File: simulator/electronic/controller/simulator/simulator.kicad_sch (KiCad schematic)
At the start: 9 parts, among them J1 Mover1, J2 Conn_01x06_Pin, J3 Conn_01x06_Pin, J4 Mover2, J5 Conn_01x06_Pin, J6 Rotator, J7 Conn_01x06_Pin, J8 Mover3, U1 ESP32 D1 Mini

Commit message: design schematics
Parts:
- removed J1: Mover1, Connector_JST:JST_XH_B6B-XH-A_1x06_P2.50mm_Vertical, symbol Connector:Conn_01x06_Socket
- removed J2, J3, J5, J7: Conn_01x06_Pin, symbol Connector:Conn_01x06_Pin
- removed J4: Mover2, Connector_JST:JST_XH_B6B-XH-A_1x06_P2.50mm_Vertical, symbol Connector:Conn_01x06_Socket
- removed J6: Rotator, Connector_JST:JST_XH_B6B-XH-A_1x06_P2.50mm_Vertical, symbol Connector:Conn_01x06_Socket
- removed J8: Mover3, Connector_JST:JST_XH_B6B-XH-A_1x06_P2.50mm_Vertical, symbol Connector:Conn_01x06_Socket
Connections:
- net GND: now also U1.1 (GND), U1.22 (GND), U1.33 (GND)
- net connection/SW_BOTTOM: now reaches U1.11 (IO_34)
- net connection1/DIR: now reaches U1.12 (IO_23/D7)
- net connection/DIR: now reaches U1.13 (IO_14/TMS)
- net connection1/PULSE: now reaches U1.14 (IO_05/D8)
- net 3V3: now reaches U1.16 (3V3)
- net connection2/SW_BOTTOM: now reaches U1.24 (IO_27)
- net connection2/PULSE: now reaches U1.25 (IO_22/D1/SCL)
- net connection3/PULSE: now reaches U1.26 (IO_25)
- net connection2/DIR: now reaches U1.27 (IO_21/D2/SDA)
- net connection3/DIR: now reaches U1.28 (IO_32)
- net connection2/SW_TOP: now reaches U1.29 (IO_17/D3)
- net connection3/SW_TOP: now reaches U1.30 (IO_12/TDI)
- net connection2/SW_CENTER: now reaches U1.31 (IO_16/D4)
- net connection3/SW_CENTER: now reaches U1.32 (IO_04)
- net connection3/SW_BOTTOM: now reaches U1.36 (IO_02)
- net connection1/SW_BOTTOM: now reaches U1.4 (IO_36/SVP/A0)
- net connection/SW_TOP: now reaches U1.5 (IO_39/SVN)
- net connection1/SW_CENTER: now reaches U1.6 (IO_26/D0)
- net connection/SW_CENTER: now reaches U1.7 (IO_35)
- net connection1/SW_TOP: now reaches U1.8 (IO_18/D5)
- net connection/PULSE: now reaches U1.9 (IO_33)
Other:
- added sheet Mover1 (Mover.kicad_sch)
- added sheet Mover2 (Mover.kicad_sch)
- added sheet Mover3 (Mover.kicad_sch)
- added sheet connection (connection.kicad_sch)
- added sheet connection1 (connection.kicad_sch)
- added sheet connection2 (connection.kicad_sch)
- added sheet connection3 (connection.kicad_sch)
- sheet Mover ports: added SW_BOTTOM, SW_CENTER, SW_TOP; removed PIN4, PIN5, PIN6

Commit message: update simulator
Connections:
- net connection2/DIR: now also U1.24 (IO_27); no longer U1.27 (IO_21/D2/SDA)
- net connection2/SW_BOTTOM: now also U1.27 (IO_21/D2/SDA); no longer U1.24 (IO_27)
- net connection2/SW_CENTER: now also U1.29 (IO_17/D3); no longer U1.31 (IO_16/D4)
- net connection2/SW_TOP: now also U1.31 (IO_16/D4); no longer U1.29 (IO_17/D3)
- no-connect marks 0 -> 7
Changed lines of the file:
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@@
 		(color 0 0 0 0)
 	)
+	(no_connect
+		(at 142.24 83.82)
+	)
+	(no_connect
+		(at 142.24 76.2)
+	)
+	(no_connect
+		(at 142.24 66.04)
+	)
+	(no_connect
+		(at 142.24 96.52)
+	)
+	(no_connect
+		(at 168.91 66.04)
+	)
+	(no_connect
+		(at 168.91 78.74)
+	)
+	(no_connect
+		(at 142.24 78.74)
+	)
 	(wire
 		(pts
@@
 	(wire
 		(pts
-			(xy 118.11 91.44) (xy 142.24 91.44)
-		)
-		(stroke
-			(width 0)
-			(type default)
-		)
-	)
-	(wire
-		(pts
 			(xy 91.44 127) (xy 91.44 123.19)
 		)
@@
 	(wire
 		(pts
+			(xy 135.89 114.3) (xy 142.24 114.3)
+		)
+		(stroke
+			(width 0)
+			(type default)
+		)
+	)
+	(wire
+		(pts
 			(xy 111.76 99.06) (xy 142.24 99.06)
 		)
@@
 	(wire
 		(pts
+			(xy 118.11 88.9) (xy 142.24 88.9)
+		)
+		(stroke
+			(width 0)
+			(type default)
+		)
+	)
+	(wire
+		(pts
 			(xy 50.8 123.19) (xy 58.42 123.19)
 		)
@@
 	(wire
 		(pts
+			(xy 120.65 91.44) (xy 142.24 91.44)
+		)
+		(stroke
+			(width 0)
+			(type default)
+		)
+	)
+	(wire
+		(pts
 			(xy 38.1 113.03) (xy 58.42 113.03)
 		)
@@
 	(wire
 		(pts
-			(xy 120.65 88.9) (xy 142.24 88.9)
-		)
-		(stroke
-			(width 0)
-			(type default)
-		)
-	)
-	(wire
-		(pts
 			(xy 38.1 85.09) (xy 58.42 85.09)
 		)
@@
 	(wire
 		(pts
-			(xy 95.25 127) (xy 142.24 127)
-		)
-		(stroke
-			(width 0)
-			(type default)
-		)
-	)
-	(wire
-		(pts
-			(xy 93.98 114.3) (xy 142.24 114.3)
-		)
-		(stroke
-			(width 0)
-			(type default)
-		)
-	)
-	(wire
-		(pts
-			(xy 95.25 118.11) (xy 95.25 127)
-		)
-		(stroke
-			(width 0)
-			(type default)
-		)
-	)
-	(wire
-		(pts
 			(xy 102.87 124.46) (xy 102.87 85.09)
 		)
@@
 	(wire
 		(pts
-			(xy 90.17 118.11) (xy 95.25 118.11)
+			(xy 90.17 118.11) (xy 135.89 118.11)
 		)
 		(stroke
@@
 	(wire
 		(pts
-			(xy 118.11 113.03) (xy 118.11 91.44)
+			(xy 118.11 88.9) (xy 118.11 113.03)
 		)
 		(stroke
@@
 	(wire
 		(pts
+			(xy 93.98 127) (xy 142.24 127)
+		)
+		(stroke
+			(width 0)
+			(type default)
+		)
+	)
+	(wire
+		(pts
 			(xy 90.17 80.01) (xy 100.33 80.01)
 		)
@@
 	(wire
 		(pts
-			(xy 120.65 115.57) (xy 120.65 88.9)
+			(xy 135.89 118.11) (xy 135.89 114.3)
+		)
+		(stroke
+			(width 0)
+			(type default)
+		)
+	)
+	(wire
+		(pts
+			(xy 120.65 115.57) (xy 120.65 91.44)
 		)
 		(stroke
@@
 	(wire
 		(pts
-			(xy 93.98 110.49) (xy 93.98 114.3)
-		)
-		(stroke
+			(xy 93.98 110.49) (xy 93.98 127)
+		)
+		(stroke

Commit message: update simulator
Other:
- sheet connection ports: added none; removed ALARM, ALARM_O
- sheet connection1 ports: added none; removed ALARM, ALARM_O
- sheet connection2 ports: added none; removed ALARM, ALARM_O
- sheet connection3 ports: added none; removed ALARM, ALARM_O
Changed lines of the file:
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@@
-			)
-		)
-		(pin "ALARM_O" output
-			(at 58.42 120.65 180)
-			(effects
-				(font
-					(size 1.27 1.27)
-				)
-				(justify left)
 			)
 		)
 		(pin "3V3" input
 			(at 90.17 105.41 0)
-			(effects
-				(font
-					(size 1.27 1.27)
-				)
-				(justify right)
-			)
-		)
-		(pin "ALARM" input
-			(at 90.17 120.65 0)
 			(effects
 				(font
@@
 			)
 		)
-		(pin "ALARM_O" output
-			(at 58.42 59.69 180)
-			(effects
-				(font
-					(size 1.27 1.27)
-				)
-				(justify left)
-			)
-		)
 		(pin "3V3" input
 			(at 90.17 44.45 0)
-			(effects
-				(font
-					(size 1.27 1.27)
-				)
-				(justify right)
-			)
-		)
-		(pin "ALARM" input
-			(at 90.17 59.69 0)
 			(effects
 				(font
@@
 			)
 		)
-		(pin "ALARM_O" output
-			(at 58.42 151.13 180)
-			(effects
-				(font
-					(size 1.27 1.27)
-				)
-				(justify left)
-			)
-		)
 		(pin "3V3" input
 			(at 90.17 135.89 0)
-			(effects
-				(font
-					(size 1.27 1.27)
-				)
-				(justify right)
-			)
-		)
-		(pin "ALARM" input
-			(at 90.17 151.13 0)
 			(effects
 				(font
@@
 			)
 		)
-		(pin "ALARM_O" output
-			(at 58.42 90.17 180)
-			(effects
-				(font
-					(size 1.27 1.27)
-				)
-				(justify left)
-			)
-		)
 		(pin "3V3" input
 			(at 90.17 74.93 0)
 			(effects
 				(font
-					(size 1.27 1.27)
-				)
-				(justify right)
-			)
-		)
-		(pin "ALARM" input
-			(at 90.17 90.17 0)
-			(effects
-				(font

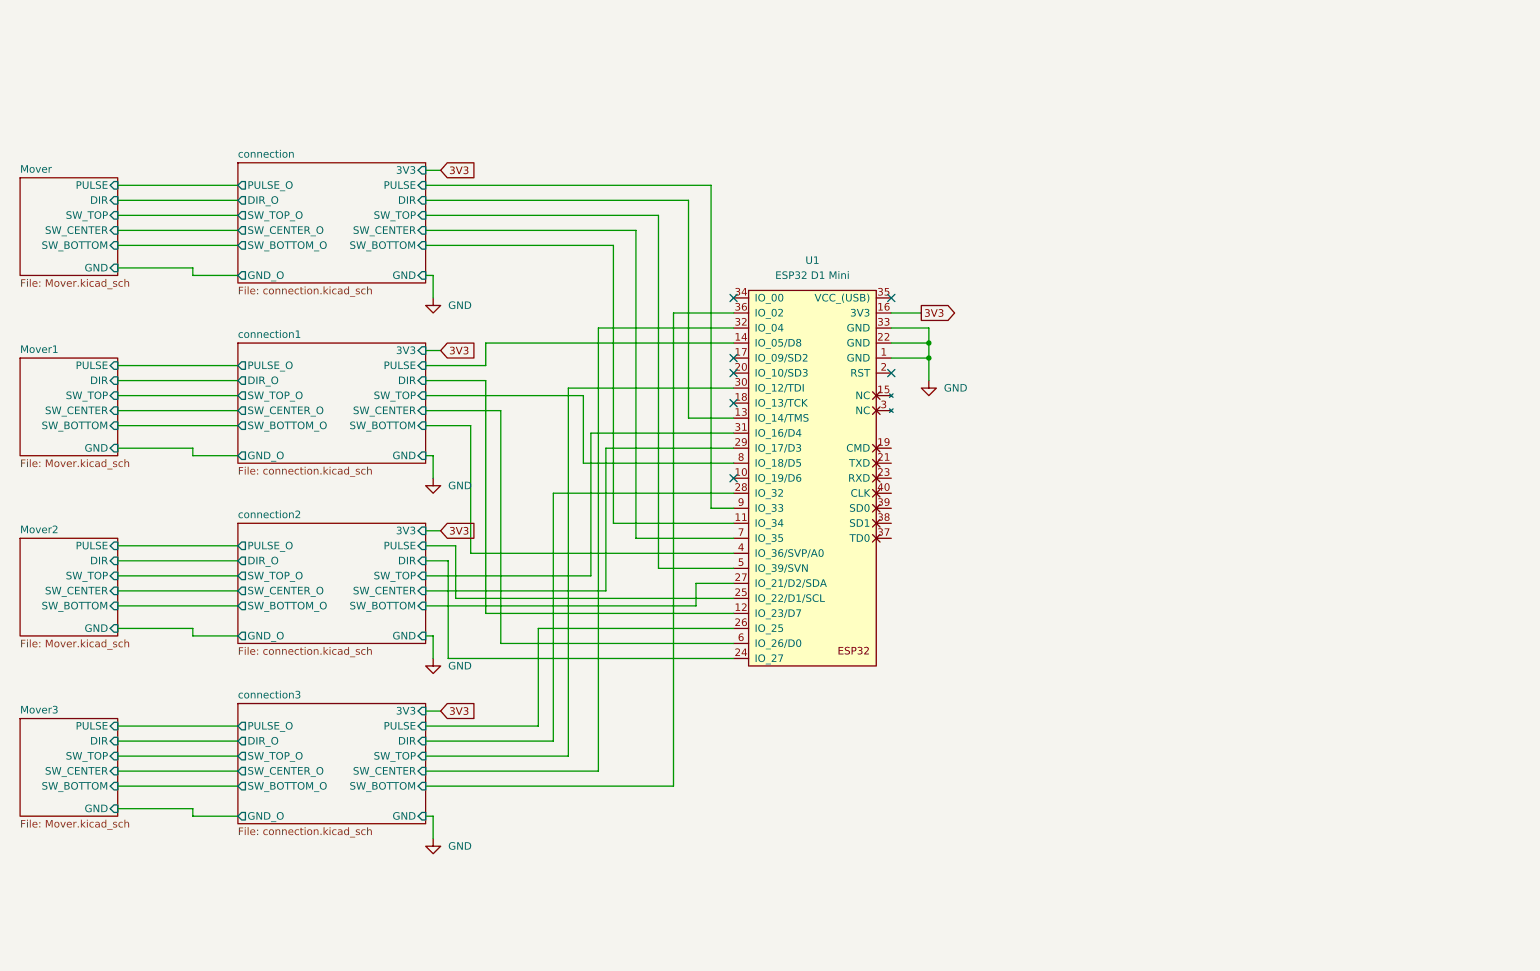
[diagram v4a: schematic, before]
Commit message: shaped schematic and PCB added printed documentation of PCB
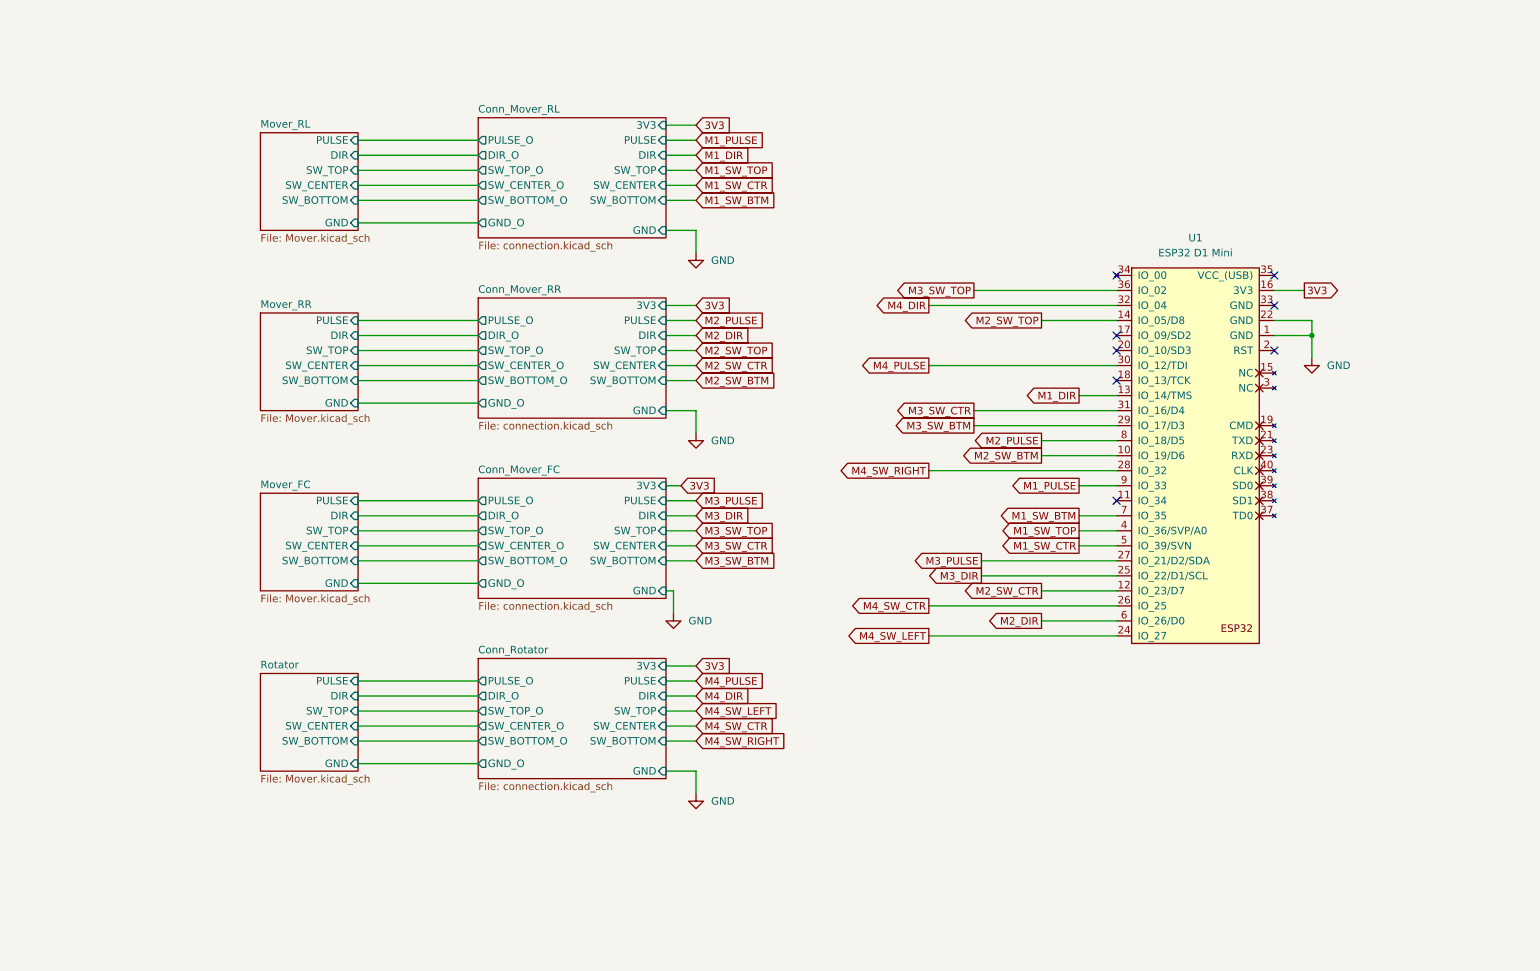
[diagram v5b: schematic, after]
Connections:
- net GND: no longer U1.33 (GND)
- net M2_SW_BTM: now reaches U1.10 (IO_19/D6)
- net Conn_Mover_RL/DIR renamed M1_DIR
- net Conn_Mover_RL/PULSE renamed M1_PULSE
- net Conn_Mover_RL/SW_BOTTOM: no longer names the net of U1.11 (IO_34)
- net Conn_Mover_RL/SW_CENTER renamed M1_SW_BTM
- net Conn_Mover_RL/SW_TOP renamed M1_SW_CTR
- net Conn_Mover_RR/DIR renamed M2_SW_CTR
- net Conn_Mover_RR/PULSE renamed M2_SW_TOP
- net Conn_Mover_RR/SW_BOTTOM renamed M1_SW_TOP
- net Conn_Mover_RR/SW_CENTER renamed M2_DIR
- net Conn_Mover_RR/SW_TOP renamed M2_PULSE
- net Conn_Mover_FC/DIR renamed M4_SW_LEFT
- net Conn_Mover_FC/PULSE renamed M3_DIR
- net Conn_Mover_FC/SW_BOTTOM renamed M3_PULSE
- net Conn_Mover_FC/SW_CENTER renamed M3_SW_BTM
- net Conn_Mover_FC/SW_TOP renamed M3_SW_CTR
- net Conn_Rotator/DIR renamed M4_SW_RIGHT
- net Conn_Rotator/PULSE renamed M4_SW_CTR
- net Conn_Rotator/SW_BOTTOM renamed M3_SW_TOP
- net Conn_Rotator/SW_CENTER renamed M4_DIR
- net Conn_Rotator/SW_TOP renamed M4_PULSE
- no-connect marks 7 -> 8
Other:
- sheet Mover renamed Mover_RL
- sheet Mover1 renamed Mover_RR
- sheet Mover2 renamed Mover_FC
- sheet Mover3 renamed Rotator
- sheet connection renamed Conn_Mover_RL
- sheet connection1 renamed Conn_Mover_RR
- sheet connection2 renamed Conn_Mover_FC
- sheet connection3 renamed Conn_Rotator
- company: (none) -> HTL Leonding
- title: Unseen-Obstacles Schaltplan -> Unseen-Obstacles - Simulator Controller

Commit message: finalized schematics and PCB
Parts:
- added P1: Power Plug, symbol Connector:Conn_Plug_3P_Protected
- added PS1, PS2: LRS-350-36, symbol UO_Electrical_Components:LRS-350-36
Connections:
- new net: P1.1 (L), PS1.2 (L), PS2.2 (L)
- new net: P1.2 (N), PS1.1 (N), PS2.1 (N)
- new net: P1.3 (PE), PS1.3 (-Vo), PS2.3 (-Vo)
- new net Mover_FC/GND_PWR: PS1.3 (-Vo)
- new net Mover_FC/V_PWR: PS1.4 (+Vo)
- new net Mover_RR/GND_PWR: PS2.3 (-Vo)
- new net Mover_RR/V_PWR: PS2.4 (+Vo)
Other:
- removed sheet Rotator
- added sheet ROTATOR (Mover.kicad_sch)
- sheet Conn_Mover_FC ports: added SW_GND_O; removed none
- sheet Conn_Mover_RL ports: added SW_GND_O; removed none
- sheet Conn_Mover_RR ports: added SW_GND_O; removed none
- sheet Conn_Rotator ports: added SW_GND_O; removed none
- sheet Mover_FC ports: added GND_PWR, SD_DIR, SD_GND, SD_PULSE, SW_COMMON, V_PWR; removed DIR, GND, PULSE
- sheet Mover_RL ports: added GND_PWR, SD_DIR, SD_GND, SD_PULSE, SW_COMMON, V_PWR; removed DIR, GND, PULSE
- sheet Mover_RR ports: added GND_PWR, SD_DIR, SD_GND, SD_PULSE, SW_COMMON, V_PWR; removed DIR, GND, PULSE
- moved on the sheet: U1

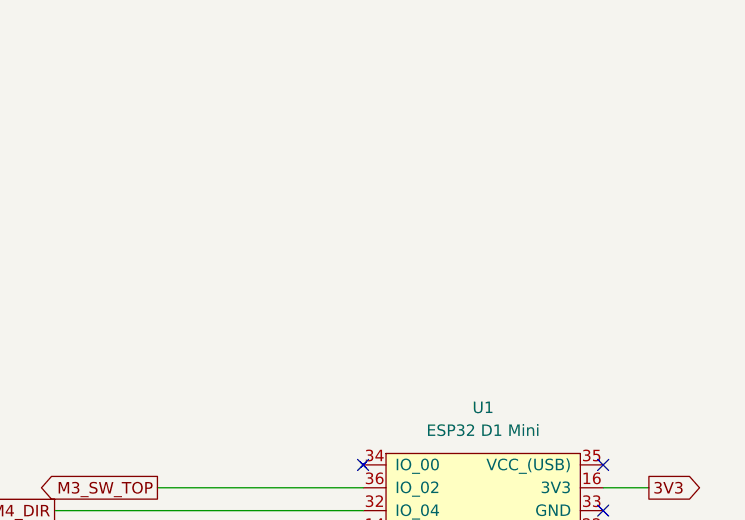
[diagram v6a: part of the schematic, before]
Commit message: added stabilization Cos and alternative text
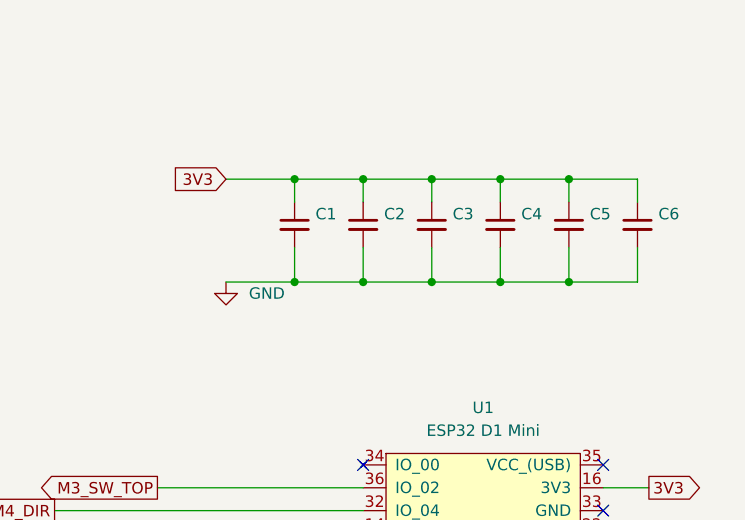
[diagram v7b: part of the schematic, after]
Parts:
- added C1, C2, C3, C4, C5, C6: 100n, Capacitor_SMD:C_0805_2012Metric_Pad1.18x1.45mm_HandSolder, symbol Device:C_Small
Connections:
- net 3V3: now also C1.1, C2.1, C3.1, C4.1, C5.1, C6.1
- net GND: now also C1.2, C2.2, C3.2, C4.2, C5.2, C6.2
- new net: P1.3 (PE), PS1.3 (-Vo), PS2.3 (-Vo)
